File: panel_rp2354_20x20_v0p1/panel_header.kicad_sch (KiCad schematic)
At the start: 4 parts, among them J2 Conn_01x05, J3 Conn_01x05, J4 Conn_01x05, J5 Conn_01x05

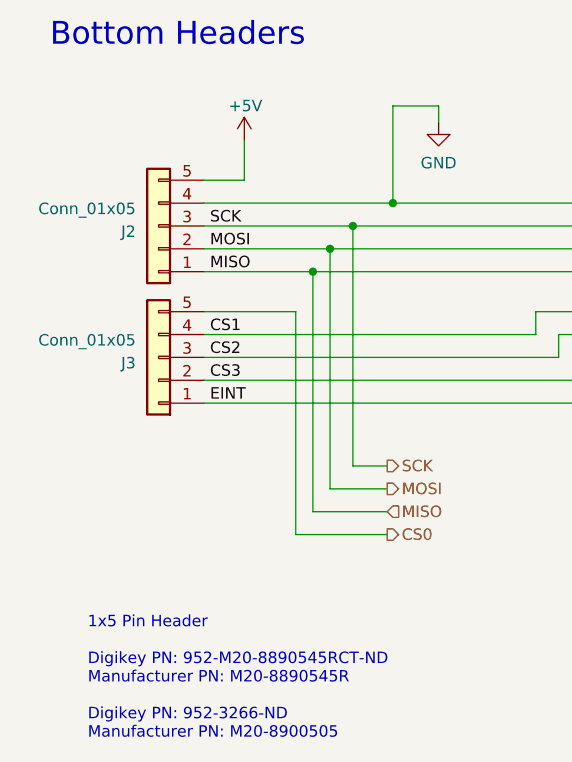
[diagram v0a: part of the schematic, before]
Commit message: Increased panel border sligthly, added production archive.
Increased the PCB border slightly (by 0.2mm on all sides) as some traces
were too close to the edge. This was easier than move the traces as
some are between the boundary and a component (typically an led).

Added production archive for previous revisions of the design.  Included
JLCPCB PCB order details and PCBA info for helping with future orders.
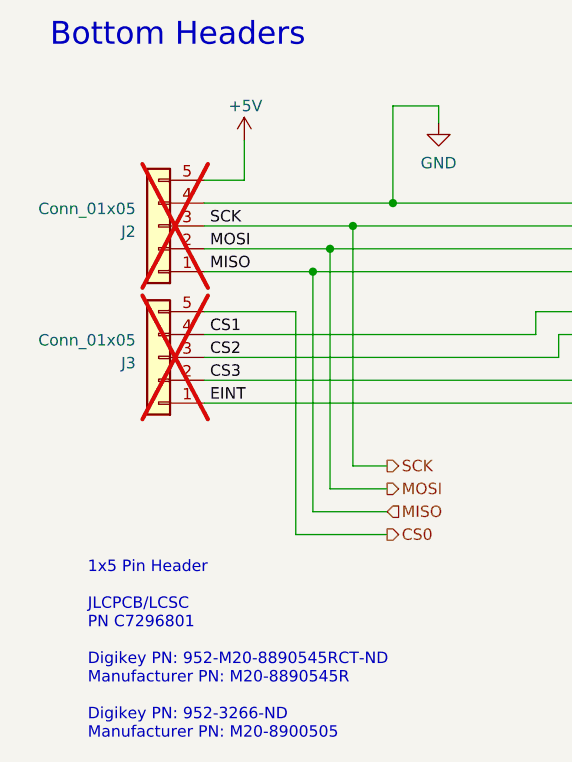
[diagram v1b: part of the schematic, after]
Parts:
- J2, J3: Digikey Part # (none) -> 952-M20-8890545RCT-ND; LCSC Part # (none) -> C7296801; now not fitted
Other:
- note added: "1x5 Pin Header JLCPCB/LCSC PN C7296801 Digikey PN: 952-M20-8890545RCT-ND Manufacturer PN: M20-8890545R Digikey PN: 952-3266-ND Manufacturer PN: M20-8900505"
- note removed: "1x5 Pin Header Digikey PN: 952-M20-8890545RCT-ND Manufacturer PN: M20-8890545R Digikey PN: 952-3266-ND Manufacturer PN: M20-8900505"
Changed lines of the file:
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@@
 	(generator_version "9.0")
 	(paper "A4")
-	(text "1x5 Pin Header\n\nDigikey PN: 952-M20-8890545RCT-ND\nManufacturer PN: M20-8890545R\n\nDigikey PN: 952-3266-ND\nManufacturer PN: M20-8900505"
+	(text "1x5 Pin Header\n\nJLCPCB/LCSC\nPN C7296801\n\nDigikey PN: 952-M20-8890545RCT-ND\nManufacturer PN: M20-8890545R\n\nDigikey PN: 952-3266-ND\nManufacturer PN: M20-8900505"
 		(exclude_from_sim no)
 		(at 91.821 147.955 0)
@@
 		(in_bom yes)
 		(on_board yes)
-		(dnp no)
+		(dnp yes)
 		(property "Reference" "J2"
 			(at 97.155 91.44 0)
@@
 			)
 		)
-		(property "LCSC Part #" ""
+		(property "LCSC Part #" "C7296801"
+			(at 99.695 90.805 0)
+			(effects
+				(font
+					(size 1.27 1.27)
+				)
+				(hide yes)
+			)
+		)
+		(property "Digikey Part #" "952-M20-8890545RCT-ND"
 			(at 99.695 90.805 0)
 			(effects
@@
 		(in_bom yes)
 		(on_board yes)
-		(dnp no)
+		(dnp yes)
 		(property "Reference" "J3"
 			(at 97.155 106.045 0)
@@
 			)
 		)
-		(property "LCSC Part #" ""
+		(property "LCSC Part #" "C7296801"
 			(at 99.695 105.41 0)
 			(effects
+				(font
+					(size 1.27 1.27)
+				)
+				(hide yes)
+			)
+		)
+		(property "Digikey Part #" "952-M20-8890545RCT-ND"
+			(at 99.695 105.41 0)
+			(effects

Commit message: prepare v0.1.3
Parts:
- J2: LCSC Alternative (none) -> C7296801; LCSC Part # C7296801 -> C46061678; now fitted
- J3: LCSC Part # C7296801 -> C46061678; LSCS Alternative (none) -> C7296801; now fitted
- J4, J5: LCSC Alternative (none) -> C21116902; LCSC Part # C21116902 -> C5142238
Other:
- note added: "1x5 Female Header Digikey PN: SMH-105-02-T-S Manufacturer PN: SMH-105-02-T-S LCSC for v0.1.3: C5142238 Manufacturer PN: X6511FRS-05-C85D30"
- note added: "1x5 Pin Header JLCPCB/LCSC PN C7296801 Digikey PN: 952-M20-8890545RCT-ND Manufacturer PN: M20-8890545R Digikey PN: 952-3266-ND Manufacturer PN: M20-8900505 LCSC for v0.1.3: C46061678 Manufacturer PN: HX PZ2.54-1x5P WT"
- note removed: "1x5 Female Header Digikey PN: SMH-105-02-T-S Manufacturer PN: SMH-105-02-T-S"
- note removed: "1x5 Pin Header JLCPCB/LCSC PN C7296801 Digikey PN: 952-M20-8890545RCT-ND Manufacturer PN: M20-8890545R Digikey PN: 952-3266-ND Manufacturer PN: M20-8900505"
- company: (none) -> IORodeo for Reiserlab @ Janelia
- title: (none) -> G6 panel 45mm RP2354
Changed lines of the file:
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@@
 	(generator_version "9.0")
 	(paper "A4")
-	(text "1x5 Pin Header\n\nJLCPCB/LCSC\nPN C7296801\n\nDigikey PN: 952-M20-8890545RCT-ND\nManufacturer PN: M20-8890545R\n\nDigikey PN: 952-3266-ND\nManufacturer PN: M20-8900505"
+	(title_block
+		(title "G6 panel 45mm RP2354")
+		(date "2025-11-25")
+		(rev "v0.1.3")
+		(company "IORodeo for Reiserlab @ Janelia")
+	)
+	(text "1x5 Pin Header\n\nJLCPCB/LCSC\nPN C7296801\n\nDigikey PN: 952-M20-8890545RCT-ND\nManufacturer PN: M20-8890545R\n\nDigikey PN: 952-3266-ND\nManufacturer PN: M20-8900505\n\nLCSC for v0.1.3: C46061678\nManufacturer PN: HX PZ2.54-1x5P WT "
 		(exclude_from_sim no)
-		(at 91.821 147.955 0)
+		(at 91.44 161.544 0)
 		(effects
 			(font
@@
 		)
 	)
-	(text "1x5 Female Header\nDigikey PN: SMH-105-02-T-S\nManufacturer PN: SMH-105-02-T-S"
+	(text "1x5 Female Header\nDigikey PN: SMH-105-02-T-S\nManufacturer PN: SMH-105-02-T-S\n\nLCSC for v0.1.3: C5142238\nManufacturer PN: X6511FRS-05-C85D30"
 		(exclude_from_sim no)
-		(at 168.275 140.97 0)
+		(at 168.656 146.812 0)
 		(effects
 			(font
@@
 			)
 		)
-		(property "LCSC Part #" "C21116902 "
+		(property "LCSC Part #" "C5142238"
+			(at 179.07 105.41 0)
+			(effects
+				(font
+					(size 1.27 1.27)
+				)
+				(hide yes)
+			)
+		)
+		(property "LCSC Alternative" "C21116902 "
 			(at 179.07 105.41 0)
 			(effects
@@
 		(in_bom yes)
 		(on_board yes)
-		(dnp yes)
+		(dnp no)
 		(property "Reference" "J2"
 			(at 97.155 91.44 0)
@@
 			)
 		)
-		(property "LCSC Part #" "C7296801"
+		(property "LCSC Part #" "C46061678"
 			(at 99.695 90.805 0)
 			(effects
@@
 		)
 		(property "Digikey Part #" "952-M20-8890545RCT-ND"
+			(at 99.695 90.805 0)
+			(effects
+				(font
+					(size 1.27 1.27)
+				)
+				(hide yes)
+			)
+		)
+		(property "LCSC Alternative" "C7296801"
 			(at 99.695 90.805 0)
 			(effects
@@
 			)
 		)
-		(property "LCSC Part #" "C21116902 "
+		(property "LCSC Part #" "C5142238"
+			(at 179.07 90.805 0)
+			(effects
+				(font
+					(size 1.27 1.27)
+				)
+				(hide yes)
+			)
+		)
+		(property "LCSC Alternative" "C21116902"
 			(at 179.07 90.805 0)
 			(effects
@@
 		(in_bom yes)
 		(on_board yes)
-		(dnp yes)
+		(dnp no)
 		(property "Reference" "J3"
 			(at 97.155 106.045 0)
@@
 			)
 		)
-		(property "LCSC Part #" "C7296801"
+		(property "LCSC Part #" "C46061678"
 			(at 99.695 105.41 0)
 			(effects
@@
 			(at 99.695 105.41 0)
 			(effects
+				(font
+					(size 1.27 1.27)
+				)
+				(hide yes)
+			)
+		)
+		(property "LSCS Alternative" "C7296801"
+			(at 99.695 105.41 0)
+			(effects

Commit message: fix conflict
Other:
- note added: "Fix EINT issue!"
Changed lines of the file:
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@@
+		)
+	)
+	(text "Fix EINT issue!"
+		(exclude_from_sim no)
+		(at 136.906 52.07 0)
+		(effects
+			(font
+				(size 5.08 5.08)
+				(thickness 0.254)
+				(bold yes)
+			)
 		)
 	)
